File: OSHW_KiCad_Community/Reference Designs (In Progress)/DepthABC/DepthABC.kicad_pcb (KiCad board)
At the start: 4 copper layers, 152 x 65.2 mm, 118 parts, among them J1 Conn_02x05_Odd_Even, J13 DF23C-50DP-0.5V_92_, J2 FAN, J3 BW1099EMB_SoM, J4 Conn_02x05_Odd_Even, J5 USBC 3.1 Vertical, J6 26_pin_FFC, J7 26_pin_FFC, J9 26_pin_FFC, Q1 RK7002B, Q2 RK7002B, Q3 RK7002B, Q4 RK7002B, Q5 RK7002B, U1 2-bit bidirectional level shi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, U6 USB Type-C Switch, U7 USB Type-C Port Control

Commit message: abc updates
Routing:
- net SD_HST0_CLK: track 92.7 -> 95.1 mm
- net MIPI_RX4_D0_N: track 75.8 -> 77.8 mm
- net SD_HST0_D3: track 96.9 -> 95.1 mm
- net MIPI_RX5_D2_P: track 75.8 -> 77.5 mm
- net MIPI_RX4_C_P: track 75.8 -> 77.5 mm
- net MIPI_RX4_C_N: track 76.0 -> 77.7 mm
- net MIPI_RX5_D2_N: track 76.0 -> 77.7 mm
- net MIPI_RX5_D3_P: track 75.9 -> 77.5 mm
- net MIPI_RX4_D0_P: track 75.9 -> 77.5 mm
- net MIPI_RX5_D3_N: track 75.8 -> 77.5 mm
- net MIPI_RX4_D1_N: track 76.0 -> 77.5 mm
- net MIPI_RX4_D1_P: track 76.0 -> 77.3 mm
- net GND: vias 100 -> 96

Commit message: abc final stages
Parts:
- removed G***: LOGO, depthABC:luxonis
- removed G***: LOGO, ABC:CE_Logo
- removed J13: DF23C-50DP-0.5V_92_, ABC:DF23C-50DS-0.5V(51)
- removed the R33 at (132.6, 122.7)
- removed the R34 at (132.1, 112.5)
- removed the R37 at (141.7, 99.6)
- removed REF**: FabDrawing-4Layer, FabDrawingTemplates:FabDrawing-4Layer-Metric_noNotes
- removed REF**: KiCad-Logo_5mm_SilkScreen-RPiModel, ABC:KiCad-Logo_5mm_SilkScreen-RPiModel
- added J8: Conn_02x25_Counter_Clockwise, ABC:DF23C-50DS-0.5V(51), F.Cu at (260.7, 118.8)
- J2: footprint Connector_JST:JST_GH_BM02B-GHS-TBT_1x02-1MP_P1.25mm_Vertical -> Connector_PinHeader_2.54mm:PinHeader_1x02_P2.54mm_Vertical
- moved J2 3.17 mm to (239.9, 102.1), turned to 90 degrees
- moved R34 0.99 mm to (223.2, 106.7)
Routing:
- net GND: track 287.8 -> 271.6 mm, vias 96 -> 97
- net /USBC&POWER/P1.15: track 34.1 -> 45.9 mm, vias 0 -> 2
- net /USBC&POWER/SCLK: track 27.4 -> 39.0 mm, vias 0 -> 2
- net /USBC&POWER/P0.30: track 32.5 -> 42.2 mm, vias 0 -> 2
- net /USBC&POWER/P1.11: track 38.4 -> 45.4 mm, vias 0 -> 2
- net /USBC&POWER/P0.31: track 28.0 -> 33.6 mm, vias 0 -> 2
- net /USBC&POWER/P0.13: track 41.4 -> 46.2 mm
- net /USBC&POWER/P1.14: track 34.9 -> 39.4 mm, vias 2 -> 0
- net /USBC&POWER/P1.03: track 32.5 -> 36.0 mm
- net 1V8: track 166.4 -> 163.5 mm
- net /USBC&POWER/P0.11: track 40.4 -> 42.8 mm
- net /USBC&POWER/VBAT: track 2.25 -> 0.00 mm
- net PMID: track 8.06 -> 6.05 mm
- net /USBC&POWER/P0.12: track 45.5 -> 47.3 mm, vias 2 -> 0
- net SD_HST0_CLK: track 95.1 -> 93.9 mm, vias 4 -> 5
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
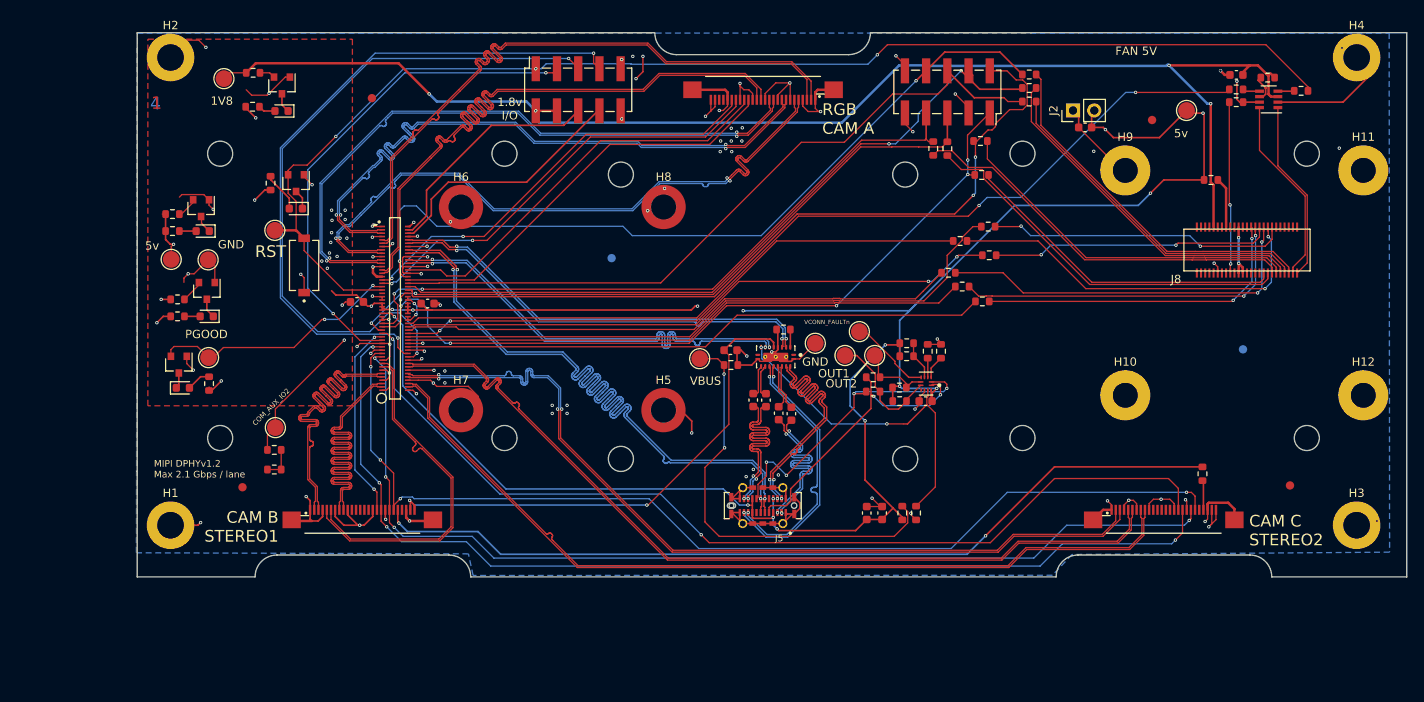
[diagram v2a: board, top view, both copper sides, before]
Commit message: abc - fixed 3.3v and 5v stuff
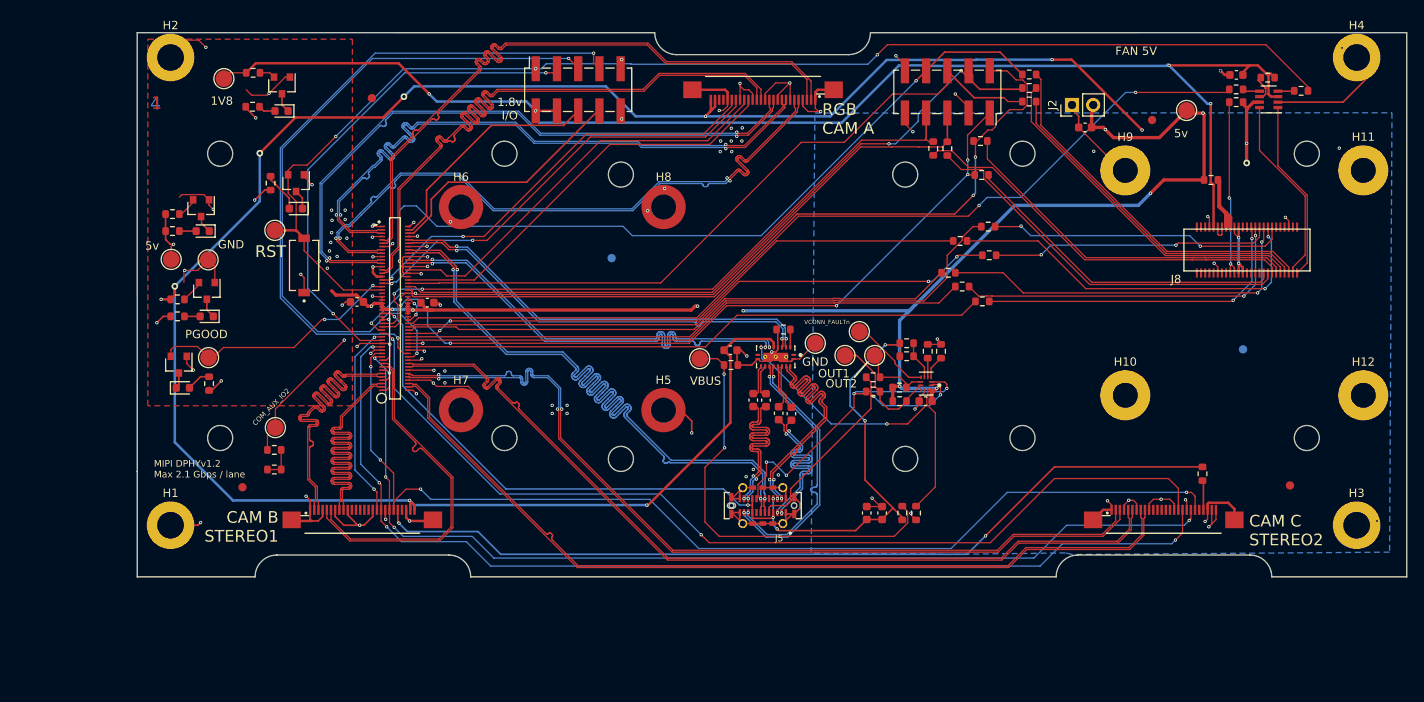
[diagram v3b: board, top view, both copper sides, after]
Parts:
- moved J2 0.67 mm to (239.8, 101.4)
- moved C3 0.10 mm to (162.6, 125.1)
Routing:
- net +3V3: track 91.7 -> 269.8 mm, vias 10 -> 13
- net GND: track 271.6 -> 276.3 mm, vias 97 -> 99
- net /USBC&POWER/VBAT: track 0.00 -> 2.33 mm
- net PMID: track 6.05 -> 7.92 mm
- net Net-(J8-Pad16): track 20.5 -> 21.8 mm
- net I2C2_SDA: track 125.0 -> 126.0 mm

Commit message: fab changes to abc
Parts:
- added G***: LOGO, Luxonis_KiCad_Master:DepthAI, B.Cu at (209.0, 164.6)
- added G***: LOGO, ABC:CE_Logo, B.Cu at (129.2, 111.2)
- added G***: LOGO, ABC:CE_Logo, F.Cu at (222.0, 144.4)
- added REF**: KiCad-Logo_8mm_SilkScreen, Symbol:KiCad-Logo_8mm_SilkScreen, F.Cu at (198.8, 132.2)
- D1, D2, D3, D4, D5: footprint Diode_SMD:D_0603_1608Metric -> LED_SMD:LED_0805_2012Metric
- R1, R2, R3, R30, R36, R4: value 1k -> 10
- U7: footprint Luxonis_KiCad_Master:Texas_Instruments-RWB0012A-0-0-MFG -> Luxonis_KiCad_Master:Texas_Instruments-TUSB321RWBR
- moved R4 21.3 mm to (129.5, 126.5)
- moved H12 19.4 mm to (260.3, 149.2)
- moved R5 19.4 mm to (242.0, 123.4)
- moved R7 19.4 mm to (252.8, 112.8)
- moved Q2 19.4 mm to (118.4, 145.5)
- moved CAM1 19.4 mm to (140.4, 137.3)
- moved CAM2 19.4 mm to (236.5, 137.3)
- moved CAM3 19.4 mm to (188.4, 139.8)
- moved MISC1 19.4 mm to (159.3, 138.8)
- moved B1 19.4 mm to (133.4, 133.7)
- moved C1 19.4 mm to (139.8, 138.0)
- moved C2 19.4 mm to (227.0, 117.1)
- moved C32 19.4 mm to (200.8, 163.3)
- moved C33 19.4 mm to (202.6, 163.3)
- moved C34 19.4 mm to (191.8, 151.4)
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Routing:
- net GND: track 276.3 -> 300.3 mm, vias 99 -> 274
- net +5V: track 179.4 -> 176.6 mm, vias 15 -> 14
- net Net-(D3-Pad2): track 4.80 -> 2.68 mm
- net SPI_SIO2: track 69.9 -> 72.0 mm
- net /USBC&POWER/P0.08: track 42.0 -> 43.7 mm
- net SD_HST0_D1: track 88.1 -> 86.5 mm
- net /USBC&POWER/P0.04: track 40.2 -> 41.7 mm
- net +3V3: track 269.8 -> 271.1 mm, vias 13 -> 24
- net I2C3_SDA: track 81.8 -> 80.9 mm
- net I2C3_SCL: track 81.0 -> 80.2 mm
- net SD_HST0_D2: track 86.6 -> 87.2 mm
- net VBUS: vias 7 -> 8
- net I2C2_SDA: vias 4 -> 5
- added copper zone on F.Cu, net GND
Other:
- board text removed: "1.8v I/O"
